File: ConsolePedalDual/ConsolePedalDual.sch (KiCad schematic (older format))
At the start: 31 parts, among them J1 AudioJack3, J2 AudioJack2, J3 Slot A, J4 Slot B, U1 CD4053B

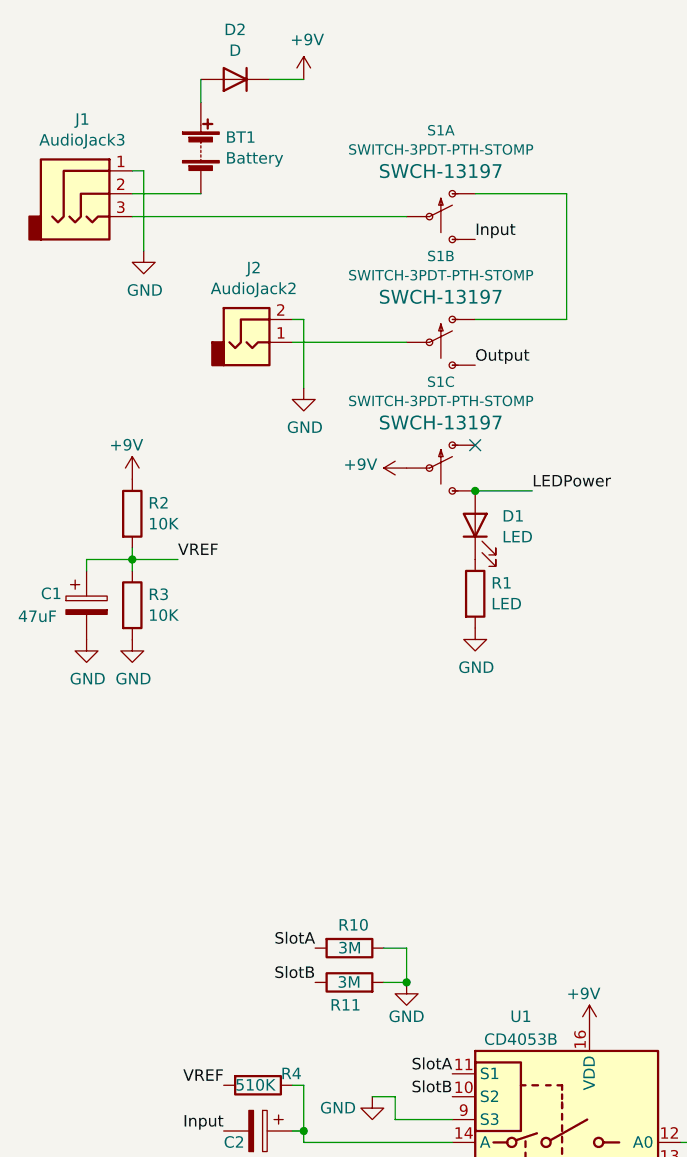
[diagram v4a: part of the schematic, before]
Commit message: Added part types to schematic
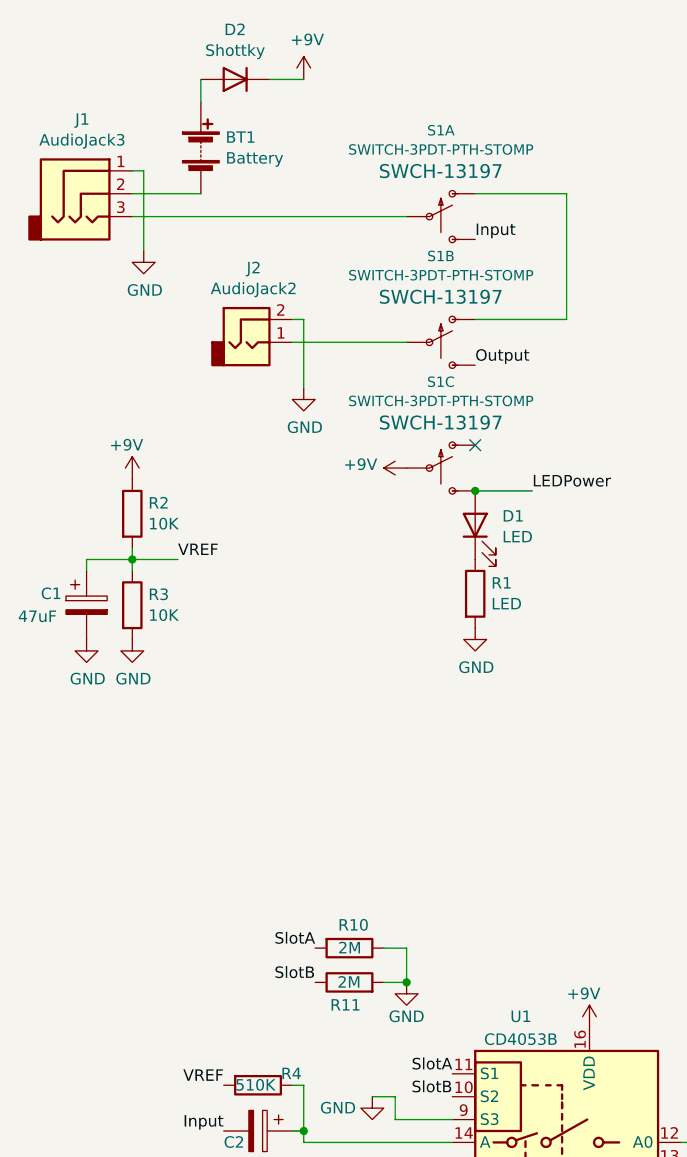
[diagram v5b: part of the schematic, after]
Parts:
- D2: value D -> Shottky
- R10, R11: value 3M -> 2M
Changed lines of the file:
@@
 P 1700 1000
 F 0 "D2" H 1700 783 50  0000 C CNN
-F 1 "D" H 1700 874 50  0000 C CNN
+F 1 "Shottky" H 1700 874 50  0000 C CNN
 F 2 "Diode_THT:D_DO-41_SOD81_P10.16mm_Horizontal" H 1700 1000 50  0001 C CNN
 F 3 "~" H 1700 1000 50  0001 C CNN
@@
 P 2200 4800
 F 0 "R10" V 2100 4750 50  0000 L CNN
-F 1 "3M" V 2200 4750 50  0000 L CNN
+F 1 "2M" V 2200 4750 50  0000 L CNN
 F 2 "Resistor_THT:R_Axial_DIN0207_L6.3mm_D2.5mm_P10.16mm_Horizontal" V 2130 4800 50  0001 C CNN
 F 3 "~" H 2200 4800 50  0001 C CNN
@@
 P 2200 4950
 F 0 "R11" V 2100 4900 50  0000 L CNN
-F 1 "3M" V 2200 4900 50  0000 L CNN
+F 1 "2M" V 2200 4900 50  0000 L CNN
 F 2 "Resistor_THT:R_Axial_DIN0207_L6.3mm_D2.5mm_P10.16mm_Horizontal" V 2130 4950 50  0001 C CNN
 F 3 "~" H 2200 4950 50  0001 C CNN
